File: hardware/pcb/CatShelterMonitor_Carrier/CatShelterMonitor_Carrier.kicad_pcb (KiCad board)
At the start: 2 copper layers, 92.9 x 115.7 mm, 12 parts, among them J1_Header1 Conn_01x06

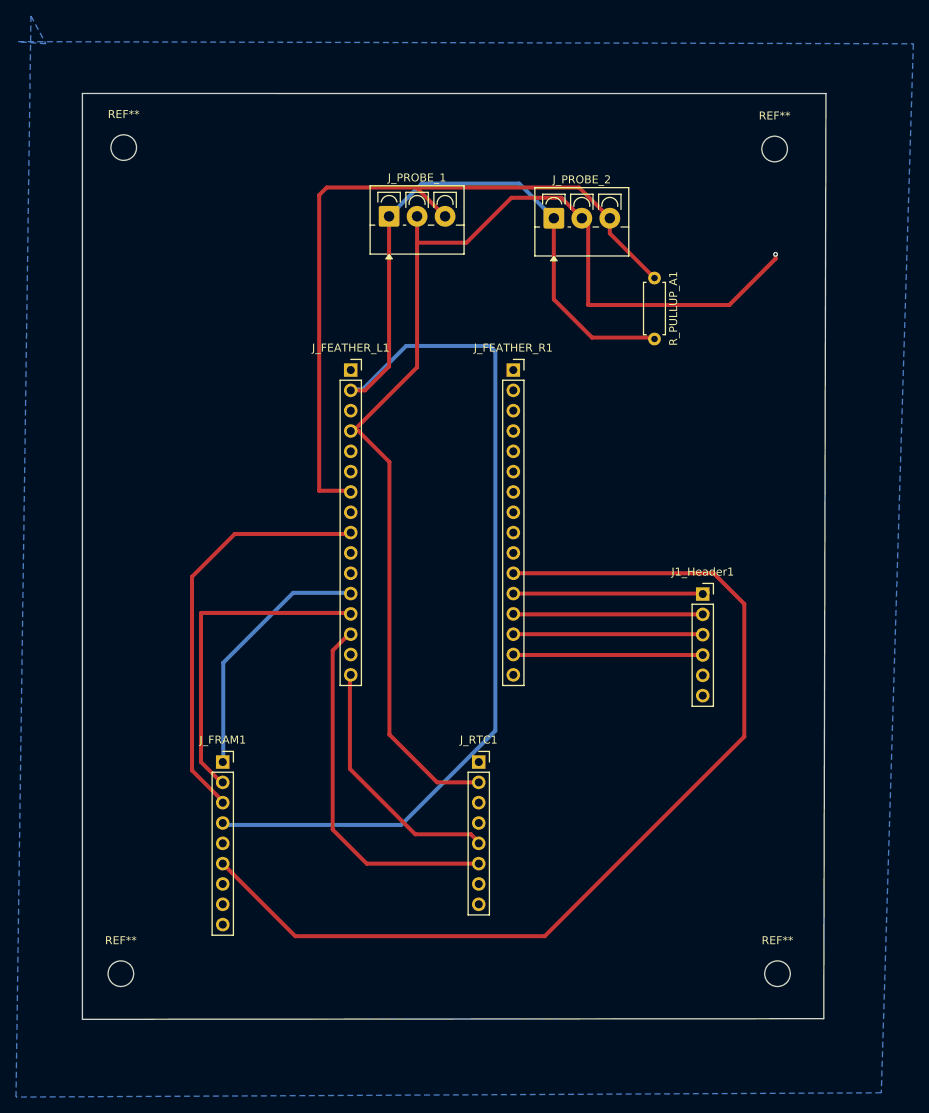
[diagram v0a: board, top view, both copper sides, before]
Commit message: Resolve footprint parity errors and verify probe routing
Corrected Schematic Parity: Updated J_PROBE_1 and J_PROBE_2 symbols to match the assigned TerminalBlock_4Ucon footprints.

Modified Symbol Library: Updated the footprint filters in Project_Connectors.kicad_sym to allow TerminalBlock* footprints, resolving persistent DRC warnings.

Verified Board Connectivity: Ran a full Design Rules Check (DRC) confirming zero violations and zero unconnected items across all nets.

Synchronized Project Files: Linked schematic values and footprints to the PCB layout using the "Update PCB from Schematic" tool with re-linking enabled.
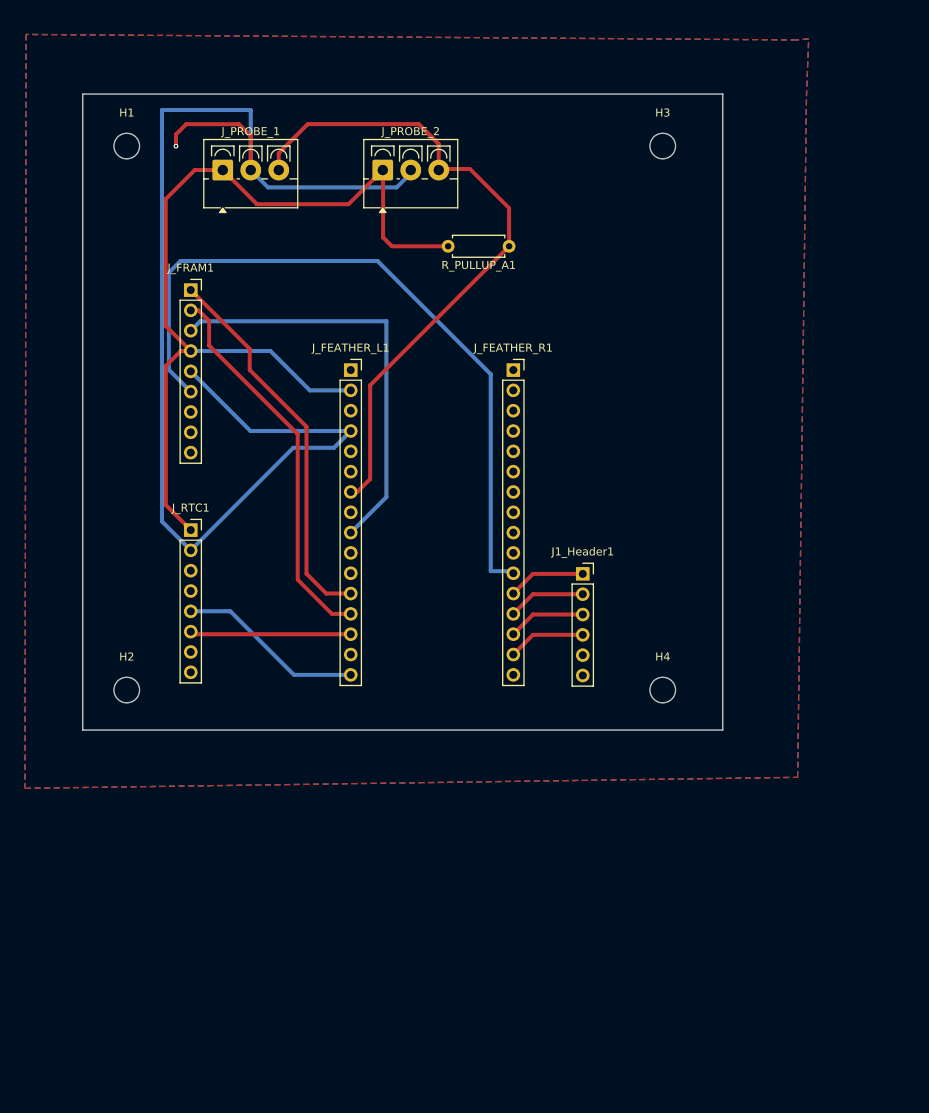
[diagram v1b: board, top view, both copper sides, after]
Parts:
- J_PROBE_1, J_PROBE_2: value Conn_01x03 -> Conn_01x03_Socket
- moved J_FRAM1 59.1 mm to (56.0, 70.0)
- moved J_RTC1 46.2 mm to (56.0, 100.0)
- moved H4 38.2 mm to (115.0, 120.0)
- moved H2 35.5 mm to (48.0, 120.0)
- moved J_PROBE_2 22.2 mm to (80.0, 55.0)
- moved J_PROBE_1 21.6 mm to (60.0, 55.0)
- moved R_PULLUP_A1 18.6 mm to (95.8, 64.5), turned to 180 degrees
- moved J1_Header1 15.2 mm to (105.0, 105.5)
- moved H3 14.0 mm to (115.0, 52.0)
- moved H1 0.43 mm to (48.0, 52.0)
- renumbered REF** to H1, REF** to H2, REF** to H3, REF** to H4
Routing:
- net +3V3: track 181.2 -> 117.2 mm
- net /FRAM_CS_D10: track 126.6 -> 90.5 mm
- net /I2C_SDA: track 45.5 -> 20.1 mm
- net GND: track 146.6 -> 163.1 mm
- net /SPI_MISO: track 32.1 -> 48.0 mm
- net Net-(J1_Header1-Pin_1): track 23.9 -> 9.87 mm
- net Net-(J1_Header1-Pin_3): track 23.7 -> 9.70 mm
- net Net-(J1_Header1-Pin_2): track 23.9 -> 9.98 mm
- net Net-(J1_Header1-Pin_4): track 23.7 -> 9.81 mm
- net /A2_1WIRE: track 94.0 -> 82.9 mm
- net /I2C_SCL: track 31.9 -> 23.3 mm
- net /SPI_MOSI: track 41.8 -> 48.2 mm
- net /SPI_SCK: track 52.2 -> 53.2 mm
- added copper zone on F.Cu, net GND
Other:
- board size 92.9 x 115.7 mm -> 80 x 79.5 mm
